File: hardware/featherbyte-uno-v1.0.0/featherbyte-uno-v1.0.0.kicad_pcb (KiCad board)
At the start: 2 copper layers, 54 x 66.8 mm, 65 parts, among them J1 Conn_01x08, J10 Conn_01x09, J2 Conn_01x10, J3 Conn_01x06, J5 USB_C_Receptacle_16P, J6 SWD Connector, J7 Terminal Block, J8 USB_C_Receptacle_16P, J9 BOOT1, SW1 Reset, SW2 BOOT0, SW3 SW_DIP_x04, U1 CH32V203CxT6, U2 TJA1050, U4 AMS1117-3.3, U5 USBLC6-2P6, U6 USBLC6-2P6, Y1 8M, Y3 32.768K

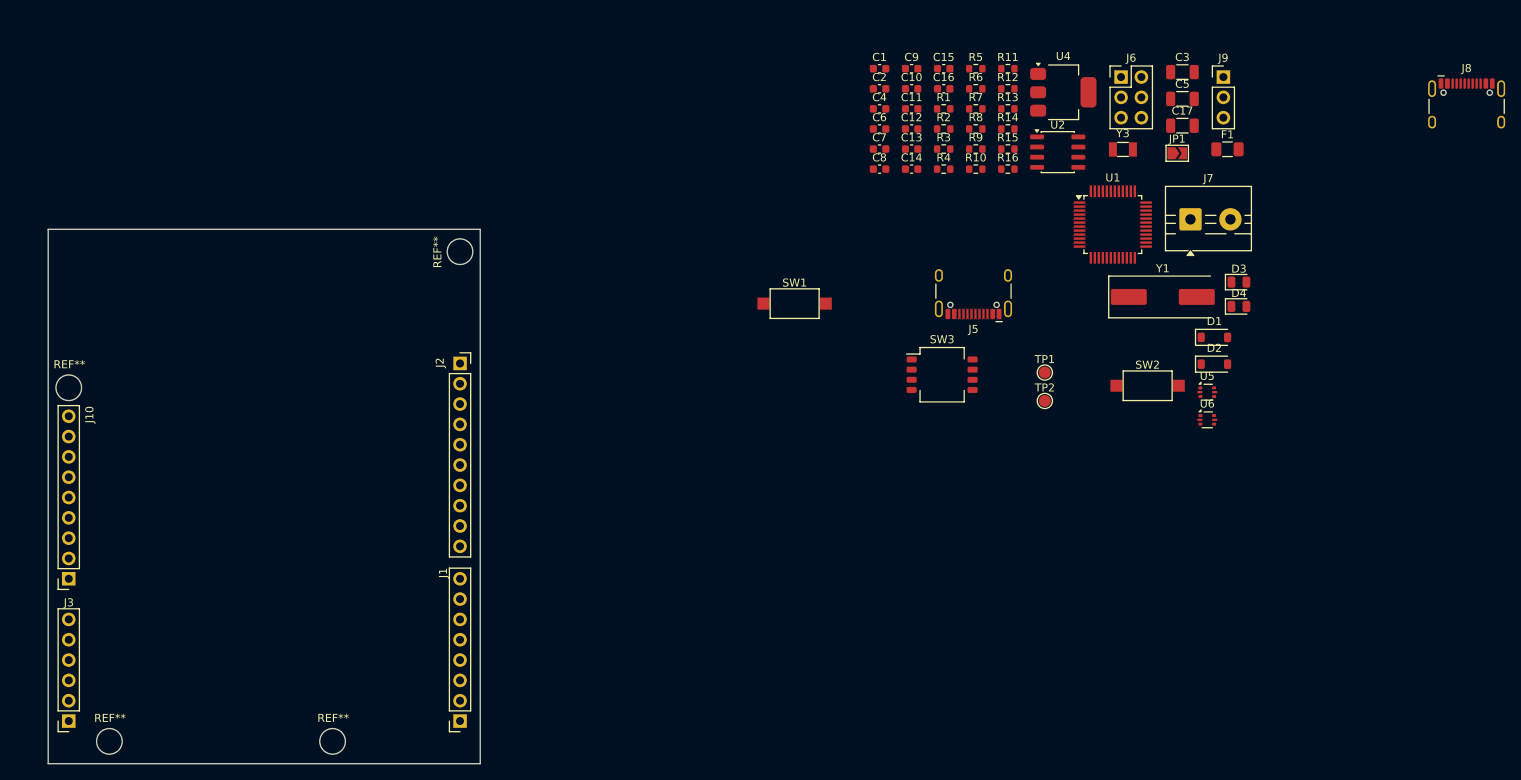
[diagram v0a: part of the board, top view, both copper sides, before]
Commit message: components are roughly placed on pcb
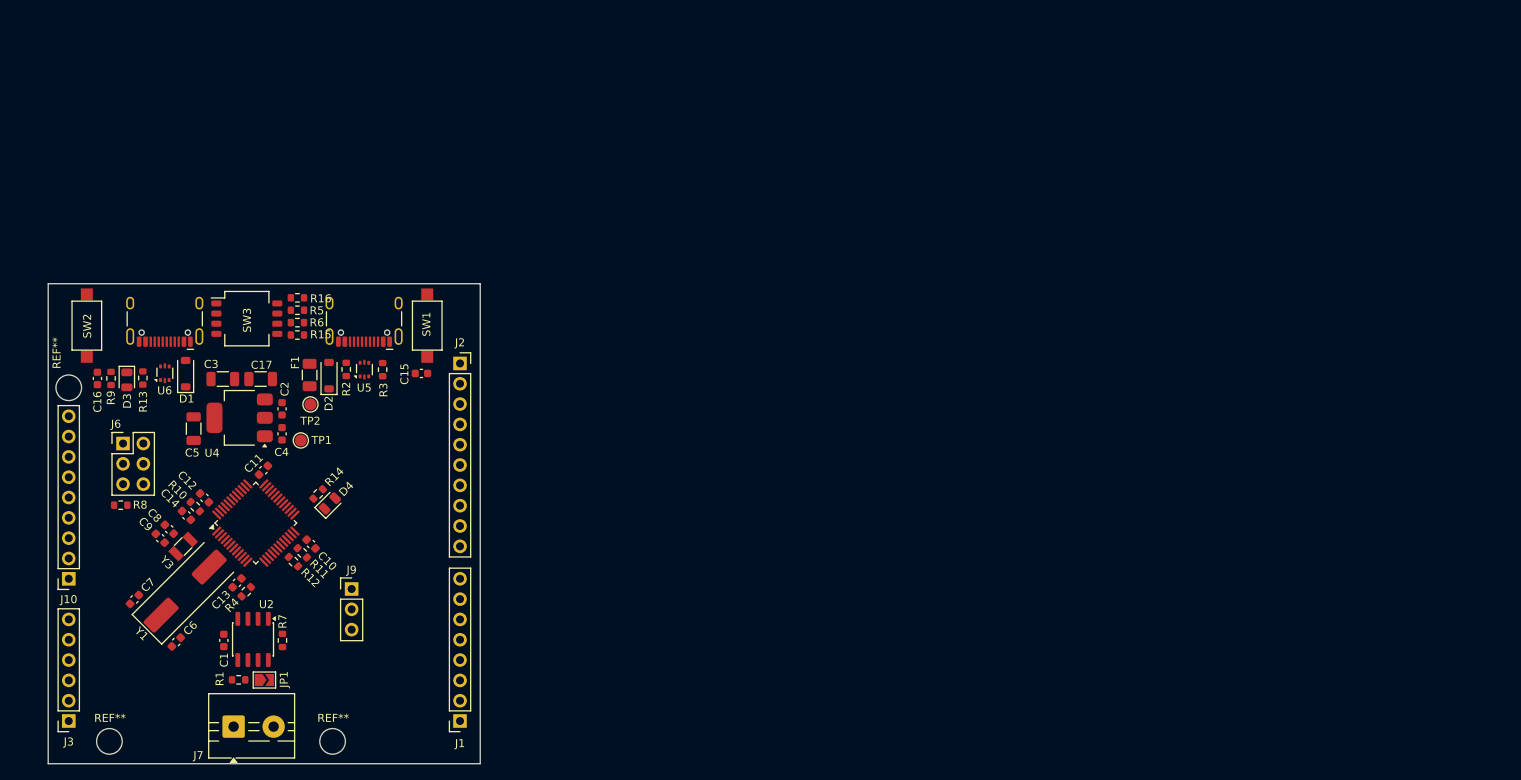
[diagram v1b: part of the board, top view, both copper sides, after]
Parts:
- removed the REF** at (119.7, 52.0)
- moved J8 140.0 mm to (107.7, 59.5), turned to 180 degrees
- moved D3 139.5 mm to (78.0, 68.0), turned to -90 degrees
- moved J7 135.4 mm to (91.3, 111.4)
- moved J6 132.9 mm to (77.5, 76.0)
- moved SW2 132.8 mm to (73.0, 61.2), turned to 90 degrees
- moved JP1 131.7 mm to (95.2, 105.5)
- moved U6 130.4 mm to (82.8, 67.2), turned to 90 degrees
- moved C5 130.3 mm to (86.3, 74.1), turned to -90 degrees
- moved D1 128.7 mm to (85.3, 67.2), turned to 90 degrees
- moved Y1 127.6 mm to (85.3, 94.4), turned to 45 degrees
- moved Y3 127.5 mm to (85.0, 88.8), turned to 45 degrees
- moved J9 126.4 mm to (106.1, 94.2)
- moved C3 125.9 mm to (90.0, 67.9), turned to 180 degrees
- moved C17 119.5 mm to (94.7, 67.9)
- moved F1 118.1 mm to (100.8, 67.4), turned to -90 degrees
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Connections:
- J5 pad A6: Net-(J5-D+-PadA6) -> /USBH_D+
- J5 pad A7: Net-(J5-D--PadA7) -> /USBH_D-
- J5 pad B6: Net-(J5-D+-PadA6) -> /USBH_D+
- J5 pad B7: Net-(J5-D--PadA7) -> /USBH_D-
- J7 pad 1: /CAN0H -> /CAN0L
- J7 pad 2: /CAN0L -> /CAN0H
- J8 pad A6: Net-(J8-D+-PadA6) -> /USBD_D+
- J8 pad A7: Net-(J8-D--PadA7) -> /USBD_D-
- J8 pad B6: Net-(J8-D+-PadA6) -> /USBD_D+
- J8 pad B7: Net-(J8-D--PadA7) -> /USBD_D-
- U1 pad 32: /USBD_DM -> /USBD_DN
- U1 pad 42: /USBHD_DM -> /USBHD_DN
- U5 pad 1: Net-(J8-D--PadA7) -> /USBD_DN
- U5 pad 3: Net-(J8-D+-PadA6) -> /USBD_DP
- U5 pad 4: /USBD_DP -> /USBD_D+
- U5 pad 6: /USBD_DM -> /USBD_D-
- U6 pad 1: Net-(J5-D--PadA7) -> /USBHD_DN
- U6 pad 3: Net-(J5-D+-PadA6) -> /USBHD_DP
- U6 pad 4: /USBHD_DP -> /USBH_D+
- U6 pad 6: /USBHD_DM -> /USBH_D-
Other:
- board size 54 x 66.8 mm -> 54 x 60 mm

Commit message: pcb routing ongoing
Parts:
- removed the REF** at (0.00, 0.00)
- moved C6 9.13 mm to (82.0, 91.9), turned to 135 degrees
- moved J9 5.69 mm to (108.3, 88.9)
- moved C14 4.03 mm to (88.3, 82.1), turned to -45 degrees
- moved C7 3.13 mm to (80.9, 93.0), turned to 135 degrees
- moved C11 2.08 mm to (97.2, 79.4)
- moved C10 1.82 mm to (101.0, 86.7)
- moved R4 1.64 mm to (94.5, 94.9), turned to -135 degrees
- moved C1 1.63 mm to (91.8, 100.5)
- moved R7 1.63 mm to (99.1, 100.5)
- moved U2 1.63 mm to (95.4, 100.4)
- moved J7 1.63 mm to (93.0, 111.3)
- moved D4 1.54 mm to (103.7, 85.0)
- moved R14 1.54 mm to (102.3, 83.8)
- moved C13 1.38 mm to (92.8, 94.3)
- moved R11 1.36 mm to (101.3, 89.5)
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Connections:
- U5 pad 1: /USBD_DN -> /USBD_D-
- U5 pad 3: /USBD_DP -> /USBD_D+
- U5 pad 4: /USBD_D+ -> /USBD_DP
- U5 pad 6: /USBD_D- -> /USBD_DN
- U6 pad 1: /USBHD_DN -> /USBH_D-
- U6 pad 3: /USBHD_DP -> /USBH_D+
- U6 pad 4: /USBH_D+ -> /USBHD_DP
- U6 pad 6: /USBH_D- -> /USBHD_DN
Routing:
- net +3.3V: track 0.00 -> 87.6 mm
- net +5V: track 0.00 -> 68.2 mm, vias 0 -> 1
- net VBUS: track 0.00 -> 46.5 mm
- net /D4: track 0.00 -> 39.8 mm
- net /D5: track 0.00 -> 38.5 mm
- net /D6: track 0.00 -> 37.6 mm
- net /D11: track 0.00 -> 37.3 mm, vias 0 -> 1
- net /D13: track 0.00 -> 36.0 mm, vias 0 -> 1
- net /D10: track 0.00 -> 33.4 mm, vias 0 -> 2
- net /D0: track 0.00 -> 32.8 mm
- net /D7: track 0.00 -> 30.4 mm, vias 0 -> 1
- net /D2: track 0.00 -> 30.0 mm
- net /D3: track 0.00 -> 28.8 mm
- net /D8: track 0.00 -> 26.8 mm, vias 0 -> 1
- net /D9: track 0.00 -> 26.5 mm, vias 0 -> 1
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- added copper zone on B.Cu, net GND
- added copper zone on F.Cu, net GND
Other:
- rule pad_to_mask_clearance: 0 -> 0.2032

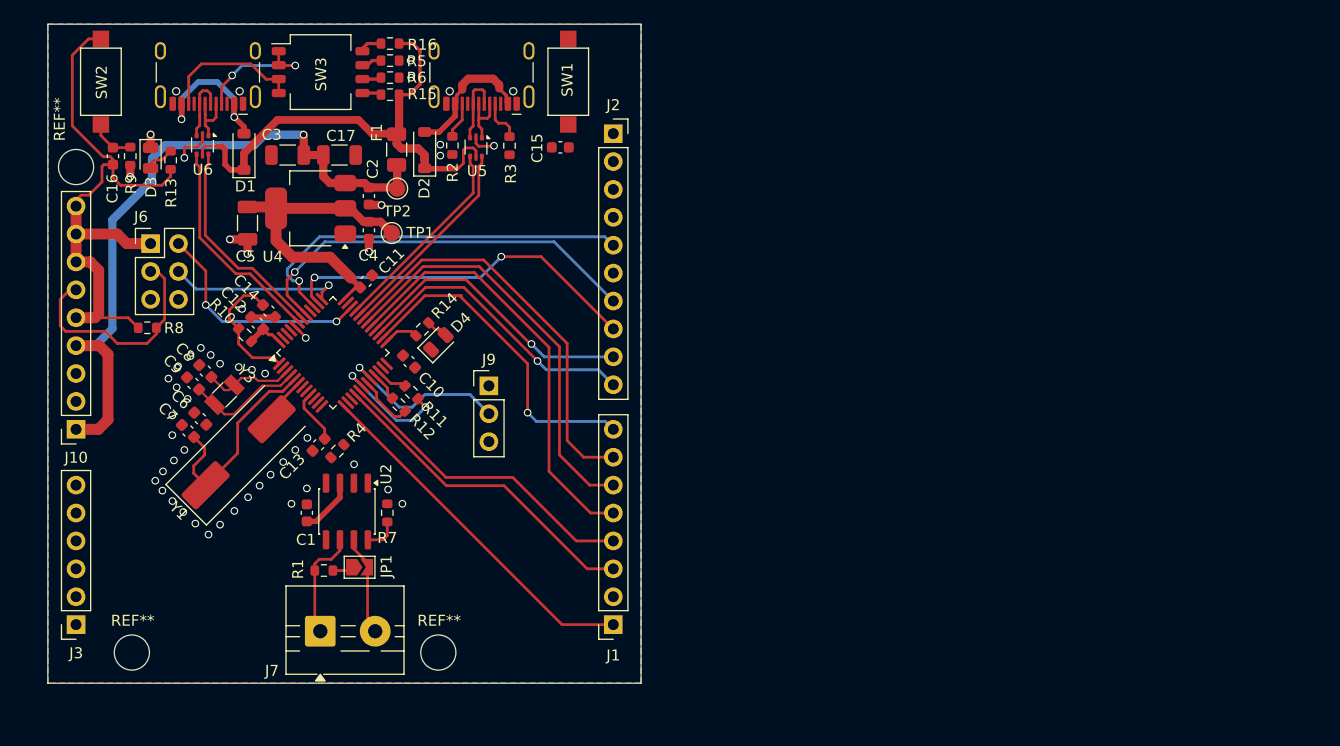
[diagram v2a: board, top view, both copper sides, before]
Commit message: restarted routing and positioning process
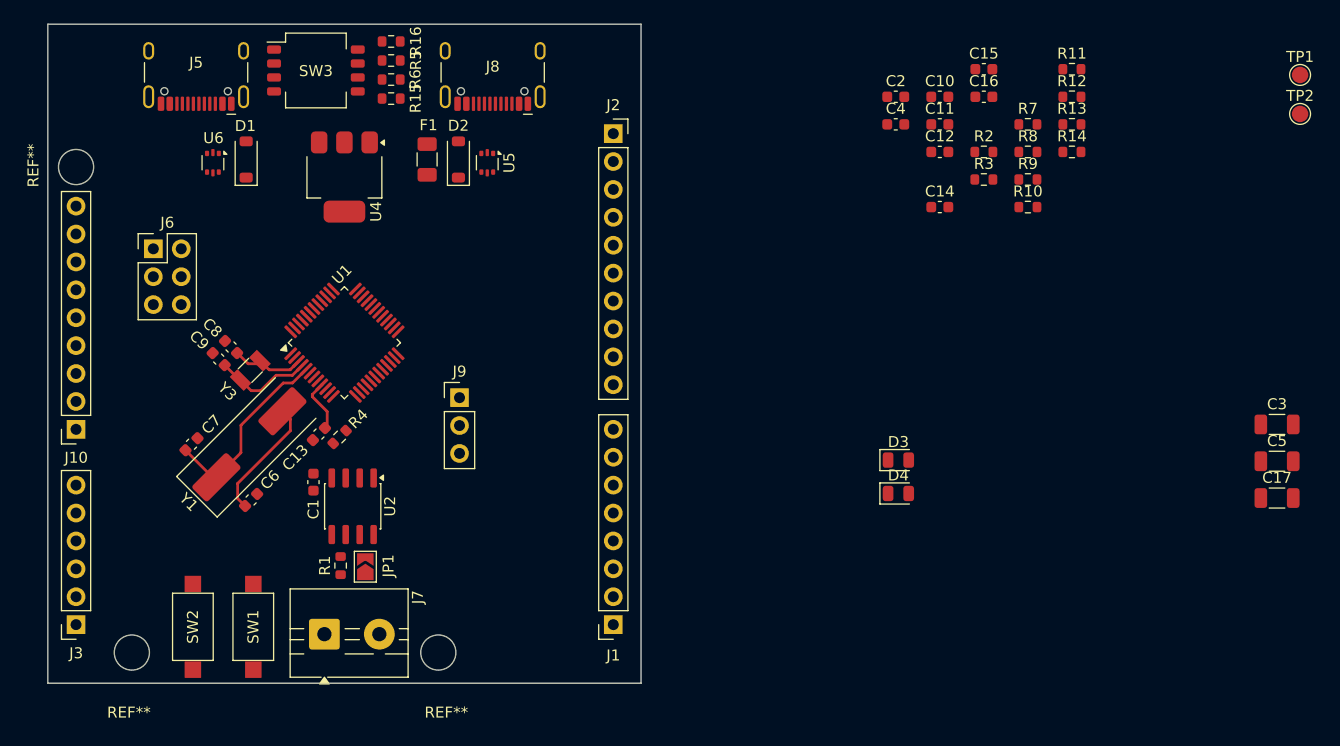
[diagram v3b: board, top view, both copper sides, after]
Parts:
- moved C5 96.2 mm to (180.1, 95.8), turned to 0 degrees
- moved C3 93.4 mm to (180.1, 92.4), turned to 0 degrees
- moved C17 90.9 mm to (180.1, 99.1)
- moved TP1 83.9 mm to (182.2, 60.6)
- moved TP2 82.5 mm to (182.2, 64.2)
- moved R13 82.1 mm to (161.4, 65.1), turned to 0 degrees
- moved R8 81.8 mm to (157.4, 67.6), turned to 0 degrees
- moved R9 81.7 mm to (157.4, 70.1), turned to 0 degrees
- moved C16 79.5 mm to (153.4, 62.6), turned to 0 degrees
- moved D3 73.4 mm to (145.6, 95.7), turned to 0 degrees
- moved R10 72.2 mm to (157.4, 72.7), turned to 0 degrees
- moved R7 68.2 mm to (157.4, 65.1), turned to 0 degrees
- moved R12 67.4 mm to (161.4, 62.6), turned to 0 degrees
- moved R11 66.9 mm to (161.4, 60.1), turned to 0 degrees
- moved C12 64.1 mm to (149.4, 67.6), turned to 0 degrees
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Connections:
- net Net-(D1-A) renamed /VBUS2
- net Net-(D2-A) renamed /VBUS1
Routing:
- net +3.3V: track 87.6 -> 0.00 mm
- net +5V: track 68.2 -> 0.00 mm, vias 1 -> 0
- net VBUS: track 46.5 -> 0.00 mm
- net /D4: track 39.8 -> 0.00 mm
- net /D5: track 38.5 -> 0.00 mm
- net /D6: track 37.6 -> 0.00 mm
- net /D11: track 37.3 -> 0.00 mm, vias 1 -> 0
- net /D13: track 36.0 -> 0.00 mm, vias 1 -> 0
- net /D10: track 33.4 -> 0.00 mm, vias 2 -> 0
- net /D0: track 32.8 -> 0.00 mm
- net /D7: track 30.4 -> 0.00 mm, vias 1 -> 0
- net /D2: track 30.0 -> 0.00 mm
- net /D3: track 28.8 -> 0.00 mm
- net /D8: track 26.8 -> 0.00 mm, vias 1 -> 0
- net /D9: track 26.5 -> 0.00 mm, vias 1 -> 0
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- removed copper zone on B.Cu, net GND
- removed copper zone on F.Cu, net GND

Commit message: footprints are roughly placed
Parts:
- moved C5 94.9 mm to (88.0, 73.0), turned to -90 degrees
- moved TP1 89.4 mm to (94.2, 76.7), turned to 90 degrees
- moved C16 88.7 mm to (76.7, 107.3), turned to 90 degrees
- moved R13 88.6 mm to (72.8, 63.5), turned to 90 degrees
- moved R9 87.4 mm to (78.3, 107.3), turned to -90 degrees
- moved TP2 86.9 mm to (95.3, 66.5)
- moved C17 84.1 mm to (100.6, 71.7)
- moved C3 81.6 mm to (100.6, 74.1)
- moved D3 81.0 mm to (72.9, 60.0), turned to -90 degrees
- moved R8 77.3 mm to (89.8, 105.1), turned to 90 degrees
- moved C15 76.6 mm to (91.4, 105.1), turned to 90 degrees
- moved R10 71.2 mm to (86.9, 82.7), turned to -45 degrees
- moved R7 68.6 mm to (99.5, 101.8), turned to 90 degrees
- moved R11 67.7 mm to (100.8, 90.2), turned to 45 degrees
- moved R12 66.0 mm to (102.0, 91.3), turned to 45 degrees
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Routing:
- net /OSC_OUT: track 11.2 -> 15.7 mm

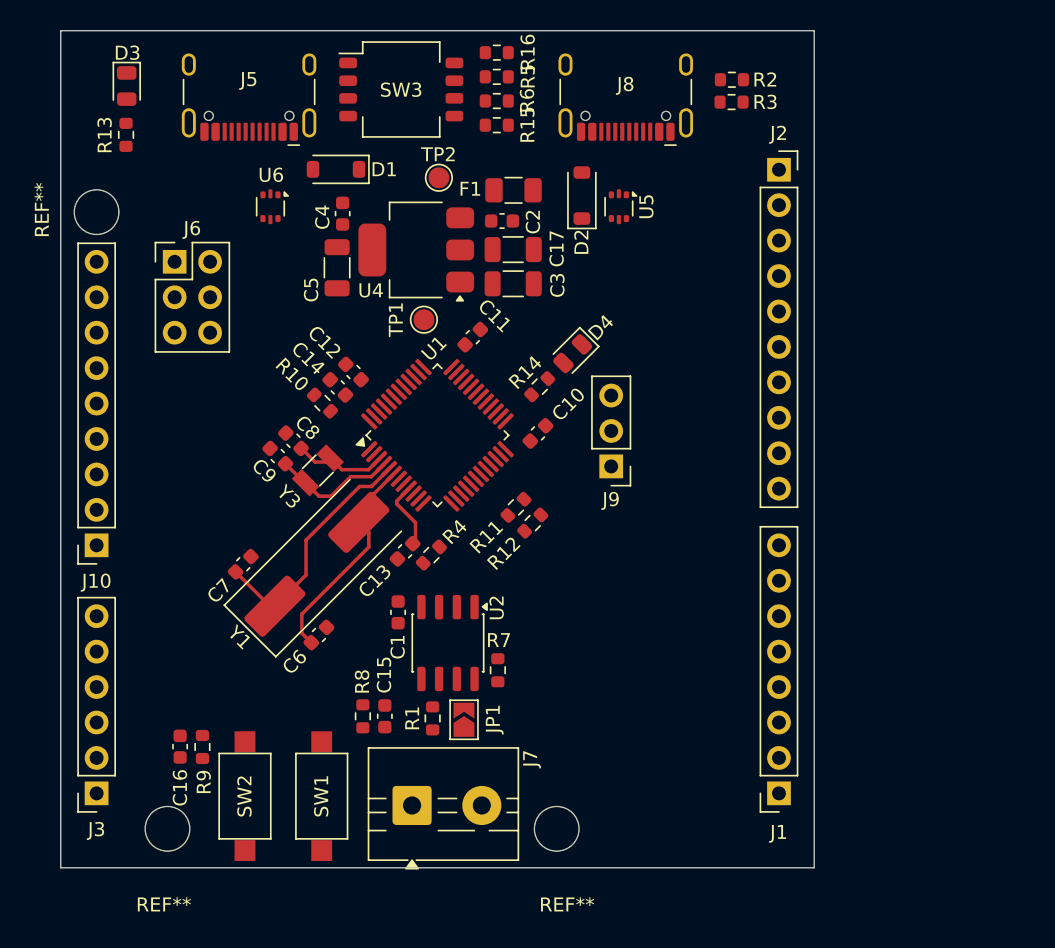
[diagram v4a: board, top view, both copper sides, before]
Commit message: pin arrangement changes required
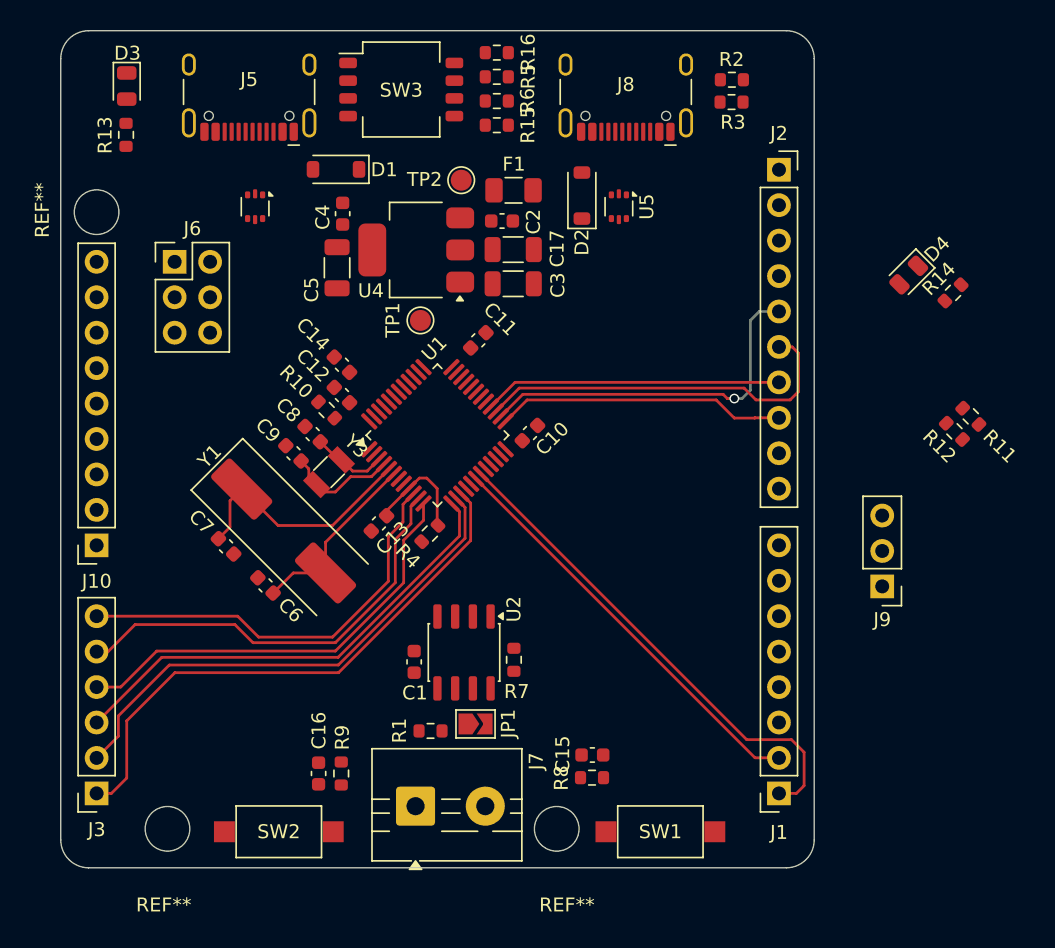
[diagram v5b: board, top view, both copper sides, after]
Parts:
- moved R11 33.2 mm to (133.4, 83.6), turned to 135 degrees
- moved R12 30.9 mm to (132.2, 84.7), turned to -45 degrees
- moved R14 30.4 mm to (132.1, 74.8)
- moved D4 24.7 mm to (128.9, 73.5)
- moved SW1 24.4 mm to (111.2, 113.4), turned to 0 degrees
- moved J9 21.2 mm to (127.0, 95.8)
- moved R8 17.0 mm to (106.2, 109.5), turned to 180 degrees
- moved C15 15.1 mm to (106.3, 107.9), turned to 180 degrees
- moved R9 10.1 mm to (88.3, 109.2)
- moved C16 10.1 mm to (86.7, 109.2)
- moved C6 5.23 mm to (82.8, 95.8), turned to 135 degrees
- moved C1 3.73 mm to (93.5, 101.2), turned to 90 degrees
- moved SW2 3.52 mm to (83.8, 113.4), turned to 180 degrees
- moved Y1 3.37 mm to (84.1, 91.9), turned to -45 degrees
- moved C13 2.74 mm to (91.0, 91.3)
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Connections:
- U1 pad 12: /D1 -> /A2
- U1 pad 13: /D0 -> /A3
- U1 pad 14: /A2 -> /A4
- U1 pad 15: /A3 -> /A5
- U1 pad 16: /D2 -> unconnected-(U1-PA6/ADC6-Pad16)
- U1 pad 17: /D3 -> unconnected-(U1-PA7/ADC7-Pad17)
- U1 pad 18: /A4 -> /D1
- U1 pad 19: /A5 -> /D0
- U1 pad 21: /SCL -> unconnected-(U1-PB10-Pad21)
- U1 pad 22: /SDA -> unconnected-(U1-PB11-Pad22)
- U1 pad 25: /LED -> /D10
- U1 pad 26: /D7 -> /D13
- U1 pad 27: /D8 -> /D12
- U1 pad 28: /D9 -> /D11
- U1 pad 29: /D4 -> unconnected-(U1-PA8-Pad29)
- U1 pad 30: /D5 -> unconnected-(U1-PA9-Pad30)
- U1 pad 31: /D6 -> unconnected-(U1-PA10-Pad31)
- U1 pad 38: /D10 -> unconnected-(U1-PA15-Pad38)
- U1 pad 39: /D13 -> unconnected-(U1-PB3-Pad39)
- U1 pad 40: /D12 -> unconnected-(U1-PB4-Pad40)
- U1 pad 41: /D11 -> unconnected-(U1-PB5-Pad41)
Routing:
- net /A5: track 0.00 -> 40.4 mm
- net /A4: track 0.00 -> 36.9 mm
- net /D0: track 0.00 -> 35.9 mm
- net /A3: track 0.00 -> 34.1 mm
- net /A2: track 0.00 -> 31.4 mm
- net /A1: track 0.00 -> 31.3 mm
- net /A0: track 0.00 -> 30.2 mm
- net /D1: track 0.00 -> 30.0 mm
- net /D12: track 0.00 -> 27.3 mm
- net /D13: track 0.00 -> 26.2 mm, vias 0 -> 1
- net /D11: track 0.00 -> 21.4 mm
- net /D10: track 0.00 -> 20.8 mm
- net /VREF: track 4.95 -> 7.89 mm
- net /OSC_OUT: track 15.7 -> 14.2 mm
- net /OSC32_IN: track 6.77 -> 5.44 mm
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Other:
- outline, holes or cut-outs redrawn
